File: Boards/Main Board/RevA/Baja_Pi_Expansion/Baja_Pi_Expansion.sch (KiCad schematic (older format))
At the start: 13 parts

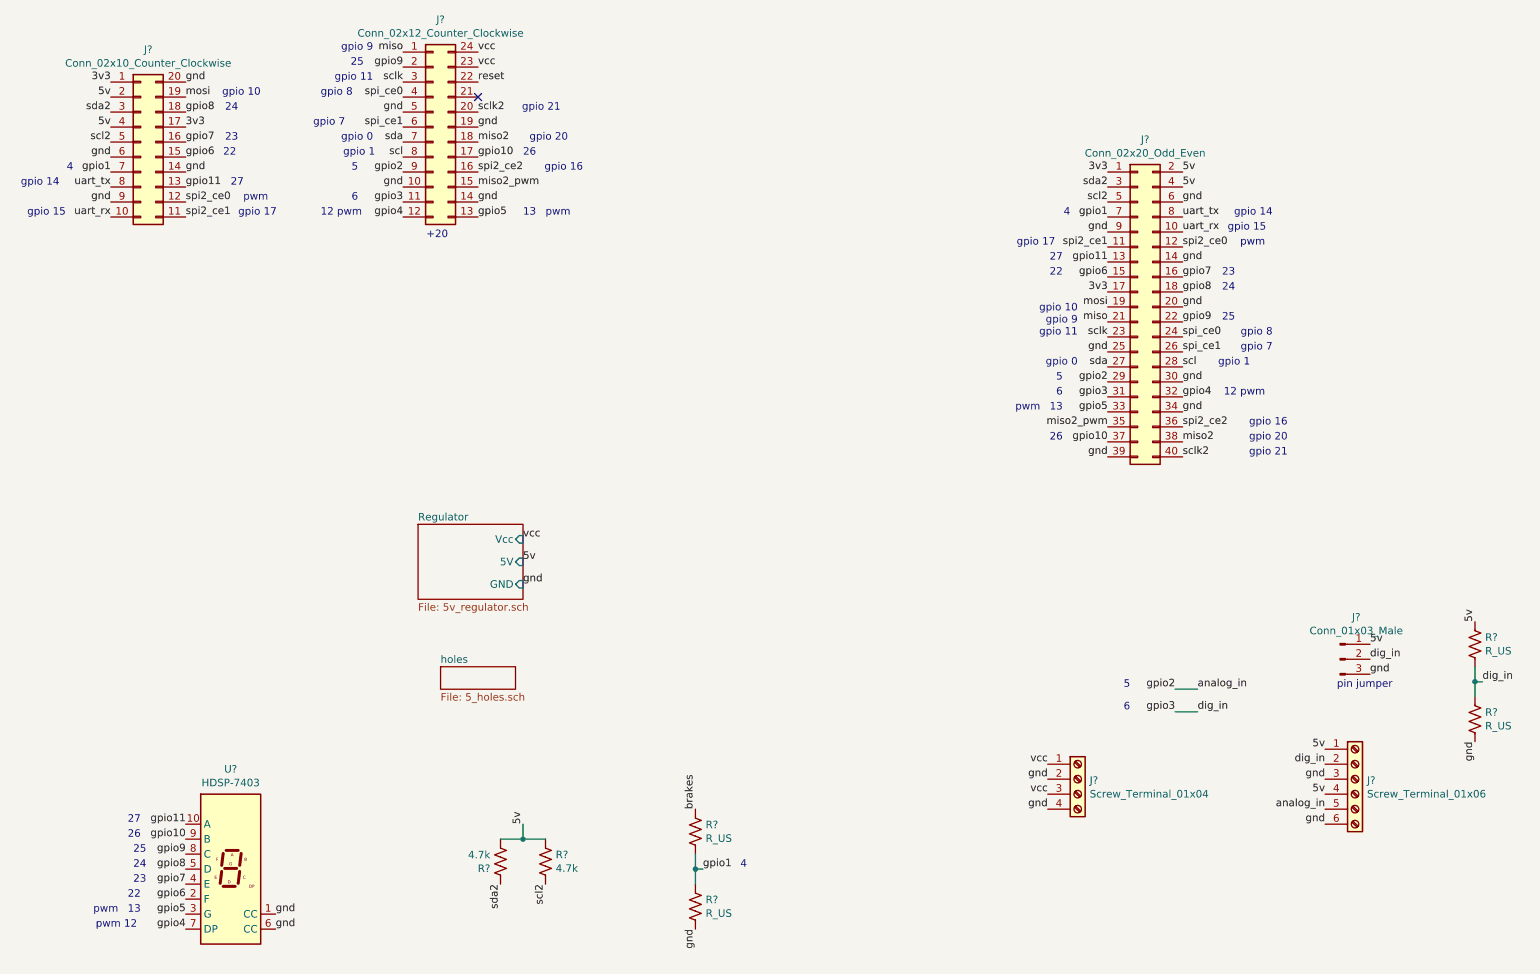
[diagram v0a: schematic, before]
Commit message: Added a Majority of Main Board Footprints
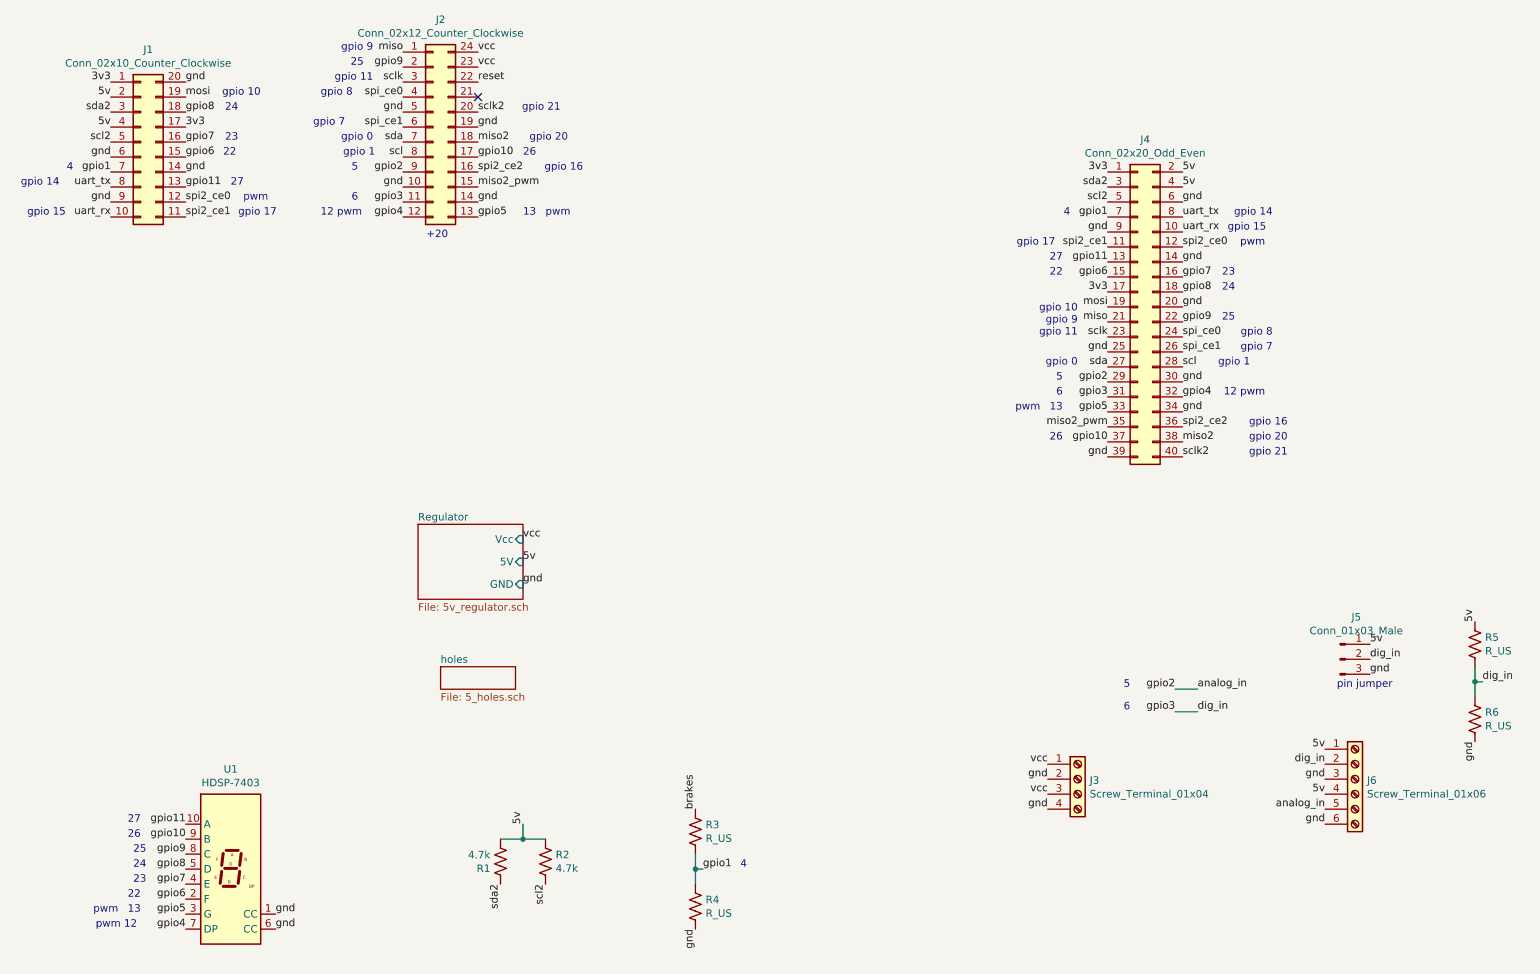
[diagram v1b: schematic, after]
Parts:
- J1: renamed from J?; footprint (none) -> Connector_PinHeader_2.54mm:PinHeader_2x10_P2.54mm_Vertical
- J2: renamed from J?; footprint (none) -> Connector_PinHeader_2.54mm:PinHeader_2x12_P2.54mm_Vertical
- J3: renamed from J?; footprint (none) -> Connector_PinHeader_2.54mm:PinHeader_1x04_P2.54mm_Vertical
- J4: renamed from J?; footprint (none) -> Connector_PinHeader_2.54mm:PinHeader_2x20_P2.54mm_Vertical
- J5: renamed from J?; footprint (none) -> Connector_PinHeader_2.54mm:PinHeader_1x03_P2.54mm_Vertical
- J6: renamed from J?; footprint (none) -> Connector_PinHeader_2.54mm:PinHeader_1x06_P2.54mm_Vertical
- R1, R2, R3, R4, R5, R6: renamed from R?; footprint (none) -> Resistor_SMD:R_0603_1608Metric
- gave numbers to parts that had none: 1
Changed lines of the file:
@@
 $EndDescr
 $Comp
-L Connector_Generic:Conn_02x20_Odd_Even J?
+L Connector_Generic:Conn_02x20_Odd_Even J4
 U 1 1 615F9685
 P 8550 2850
-F 0 "J?" H 8600 3967 50  0000 C CNN
+F 0 "J4" H 8600 3967 50  0000 C CNN
 F 1 "Conn_02x20_Odd_Even" H 8600 3876 50  0000 C CNN
-F 2 "" H 8550 2850 50  0001 C CNN
+F 2 "Connector_PinHeader_2.54mm:PinHeader_2x20_P2.54mm_Vertical" H 8550 2850 50  0001 C CNN
 F 3 "~" H 8550 2850 50  0001 C CNN
 	1    8550 2850
@@
 gpio 0
 $Comp
-L Connector_Generic:Conn_02x10_Counter_Clockwise J?
+L Connector_Generic:Conn_02x10_Counter_Clockwise J1
 U 1 1 6160E35B
 P 1900 1750
-F 0 "J?" H 1950 2367 50  0000 C CNN
+F 0 "J1" H 1950 2367 50  0000 C CNN
 F 1 "Conn_02x10_Counter_Clockwise" H 1950 2276 50  0000 C CNN
-F 2 "" H 1900 1750 50  0001 C CNN
+F 2 "Connector_PinHeader_2.54mm:PinHeader_2x10_P2.54mm_Vertical" H 1900 1750 50  0001 C CNN
 F 3 "~" H 1900 1750 50  0001 C CNN
 	1    1900 1750
@@
 $EndComp
 $Comp
-L Connector_Generic:Conn_02x12_Counter_Clockwise J?
+L Connector_Generic:Conn_02x12_Counter_Clockwise J2
 U 1 1 6160FED6
 P 3850 1650
-F 0 "J?" H 3900 2367 50  0000 C CNN
+F 0 "J2" H 3900 2367 50  0000 C CNN
 F 1 "Conn_02x12_Counter_Clockwise" H 3900 2276 50  0000 C CNN
-F 2 "" H 3850 1650 50  0001 C CNN
+F 2 "Connector_PinHeader_2.54mm:PinHeader_2x12_P2.54mm_Vertical" H 3850 1650 50  0001 C CNN
 F 3 "~" H 3850 1650 50  0001 C CNN
 	1    3850 1650
@@
 vcc
 $Comp
-L Display_Character:HDSP-7403 U?
+L Display_Character:HDSP-7403 U1
 U 1 1 61621AB7
 P 2500 6600
-F 0 "U?" H 2500 7267 50  0000 C CNN
+F 0 "U1" H 2500 7267 50  0000 C CNN
 F 1 "HDSP-7403" H 2500 7176 50  0000 C CNN
 F 2 "Display_7Segment:HDSP-7401" H 2500 6050 50  0001 C CNN
@@
 scl2
 $Comp
-L Device:R_US R?
+L Device:R_US R1
 U 1 1 6162B2A1
 P 4300 6550
-F 0 "R?" H 4232 6504 50  0000 R CNN
+F 0 "R1" H 4232 6504 50  0000 R CNN
 F 1 "4.7k" H 4232 6595 50  0000 R CNN
-F 2 "" V 4340 6540 50  0001 C CNN
+F 2 "Resistor_SMD:R_0603_1608Metric" V 4340 6540 50  0001 C CNN
 F 3 "~" H 4300 6550 50  0001 C CNN
 	1    4300 6550
@@
 $EndComp
 $Comp
-L Device:R_US R?
+L Device:R_US R2
 U 1 1 6162C8FC
 P 4600 6550
-F 0 "R?" H 4532 6504 50  0000 R CNN
+F 0 "R2" H 4532 6504 50  0000 R CNN
 F 1 "4.7k" H 4532 6595 50  0000 R CNN
-F 2 "" V 4640 6540 50  0001 C CNN
+F 2 "Resistor_SMD:R_0603_1608Metric" V 4640 6540 50  0001 C CNN
 F 3 "~" H 4600 6550 50  0001 C CNN
 	1    4600 6550
@@
 	4450 6400 4600 6400
 $Comp
-L Device:R_US R?
+L Device:R_US R3
 U 1 1 6162DB16
 P 5600 6350
-F 0 "R?" H 5668 6396 50  0000 L CNN
+F 0 "R3" H 5668 6396 50  0000 L CNN
 F 1 "R_US" H 5668 6305 50  0000 L CNN
-F 2 "" V 5640 6340 50  0001 C CNN
+F 2 "Resistor_SMD:R_0603_1608Metric" V 5640 6340 50  0001 C CNN
 F 3 "~" H 5600 6350 50  0001 C CNN
 	1    5600 6350
@@
 $EndComp
 $Comp
-L Device:R_US R?
+L Device:R_US R4
 U 1 1 6162E182
 P 5600 6850
-F 0 "R?" H 5668 6896 50  0000 L CNN
+F 0 "R4" H 5668 6896 50  0000 L CNN
 F 1 "R_US" H 5668 6805 50  0000 L CNN
-F 2 "" V 5640 6840 50  0001 C CNN
+F 2 "Resistor_SMD:R_0603_1608Metric" V 5640 6840 50  0001 C CNN
 F 3 "~" H 5600 6850 50  0001 C CNN
 	1    5600 6850
@@
 	5600 6600 5600 6500
 $Comp
-L Connector:Screw_Terminal_01x06 J?
+L Connector:Screw_Terminal_01x06 J6
 U 1 1 61634923
 P 10000 6000
-F 0 "J?" H 10080 5992 50  0000 L CNN
+F 0 "J6" H 10080 5992 50  0000 L CNN
 F 1 "Screw_Terminal_01x06" H 10080 5901 50  0000 L CNN
-F 2 "" H 10000 6000 50  0001 C CNN
+F 2 "Connector_PinHeader_2.54mm:PinHeader_1x06_P2.54mm_Vertical" H 10000 6000 50  0001 C CNN
 F 3 "~" H 10000 6000 50  0001 C CNN
 	1    10000 6000
@@
 $EndComp
 $Comp
-L Connector:Screw_Terminal_01x04 J?
+L Connector:Screw_Terminal_01x04 J3
 U 1 1 61635B3A
 P 8150 6000
-F 0 "J?" H 8230 5992 50  0000 L CNN
+F 0 "J3" H 8230 5992 50  0000 L CNN
 F 1 "Screw_Terminal_01x04" H 8230 5901 50  0000 L CNN
-F 2 "" H 8150 6000 50  0001 C CNN
+F 2 "Connector_PinHeader_2.54mm:PinHeader_1x04_P2.54mm_Vertical" H 8150 6000 50  0001 C CNN
 F 3 "~" H 8150 6000 50  0001 C CNN
 	1    8150 6000
@@
 vcc
 $Comp
-L Connector:Conn_01x03_Male J?
+L Connector:Conn_01x03_Male J5
 U 1 1 61637A7E
 P 9900 5200
-F 0 "J?" H 10008 5481 50  0000 C CNN
+F 0 "J5" H 10008 5481 50  0000 C CNN
 F 1 "Conn_01x03_Male" H 10008 5390 50  0000 C CNN
-F 2 "" H 9900 5200 50  0001 C CNN
+F 2 "Connector_PinHeader_2.54mm:PinHeader_1x03_P2.54mm_Vertical" H 9900 5200 50  0001 C CNN
 F 3 "~" H 9900 5200 50  0001 C CNN
 	1    9900 5200
@@
 analog_in
 $Comp
-L Device:R_US R?
+L Device:R_US R5
 U 1 1 6163FA23
 P 10800 5100
-F 0 "R?" H 10868 5146 50  0000 L CNN
+F 0 "R5" H 10868 5146 50  0000 L CNN
 F 1 "R_US" H 10868 5055 50  0000 L CNN
-F 2 "" V 10840 5090 50  0001 C CNN
+F 2 "Resistor_SMD:R_0603_1608Metric" V 10840 5090 50  0001 C CNN
 F 3 "~" H 10800 5100 50  0001 C CNN
 	1    10800 5100
@@
 $EndComp
 $Comp
-L Device:R_US R?
+L Device:R_US R6
 U 1 1 6163FA29
 P 10800 5600
-F 0 "R?" H 10868 5646 50  0000 L CNN
+F 0 "R6" H 10868 5646 50  0000 L CNN
 F 1 "R_US" H 10868 5555 50  0000 L CNN
-F 2 "" V 10840 5590 50  0001 C CNN
+F 2 "Resistor_SMD:R_0603_1608Metric" V 10840 5590 50  0001 C CNN
 F 3 "~" H 10800 5600 50  0001 C CNN
 	1    10800 5600

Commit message: Added \#Parts
(For 5V Regulator)
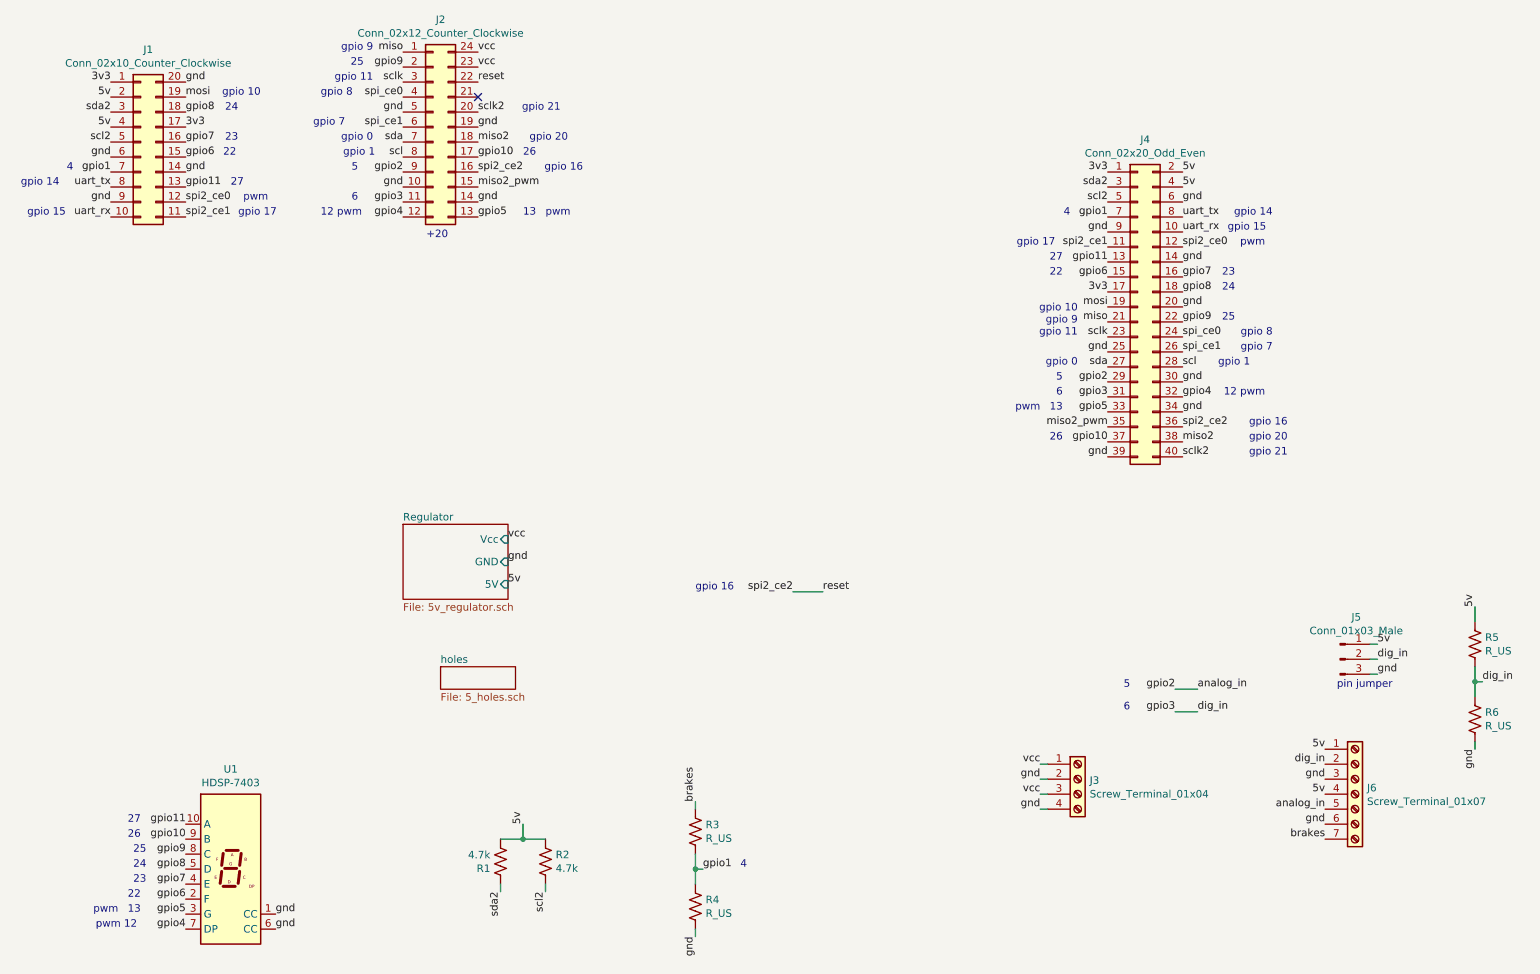
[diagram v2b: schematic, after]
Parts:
- removed J6: Screw_Terminal_01x06, Connector_PinHeader_2.54mm:PinHeader_1x06_P2.54mm_Vertical, symbol Connector:Screw_Terminal_01x06
- added J6: Screw_Terminal_01x07, Connector_PinHeader_2.54mm:PinHeader_1x07_P2.54mm_Vertical, symbol Connector:Screw_Terminal_01x07
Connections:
- net spi2_ce2 is gone; now on net reset: J2.16 (Pin_16), J4.36 (Pin_36)
- net 5v: now also J6.1 (Pin_1), J6.4 (Pin_4)
- net analog_in: now also J6.5 (Pin_5)
- net brakes: now also J6.7 (Pin_7)
- net dig_in: now also J6.2 (Pin_2)
- net gnd: now also J6.3 (Pin_3), J6.6 (Pin_6)
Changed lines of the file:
@@
 Text Notes 1600 7000 0    50   ~ 0
 pwm 12
-Text Label 4300 6700 3    50   ~ 0
+Text Label 4300 6750 3    50   ~ 0
 sda2
-Text Label 4600 6700 3    50   ~ 0
+Text Label 4600 6750 3    50   ~ 0
 scl2
 $Comp
@@
 Wire Wire Line
 	5600 6700 5600 6600
-Text Label 5600 7000 3    50   ~ 0
-gnd
-Text Label 5600 6200 1    50   ~ 0
+Text Label 5600 7050 3    50   ~ 0
+gnd
+Text Label 5600 6150 1    50   ~ 0
 brakes
 Text Label 5650 6600 0    50   ~ 0
@@
 Wire Wire Line
 	5600 6600 5600 6500
-$Comp
-L Connector:Screw_Terminal_01x06 J6
-U 1 1 61634923
-P 10000 6000
-F 0 "J6" H 10080 5992 50  0000 L CNN
-F 1 "Screw_Terminal_01x06" H 10080 5901 50  0000 L CNN
-F 2 "Connector_PinHeader_2.54mm:PinHeader_1x06_P2.54mm_Vertical" H 10000 6000 50  0001 C CNN
-F 3 "~" H 10000 6000 50  0001 C CNN
-	1    10000 6000
-	1    0    0    -1
-$EndComp
 $Comp
 L Connector:Screw_Terminal_01x04 J3
@@
 	1    0    0    -1
 $EndComp
-Text Label 7950 6000 2    50   ~ 0
-gnd
-Text Label 7950 6200 2    50   ~ 0
-gnd
-Text Label 7950 5900 2    50   ~ 0
+Text Label 7900 6000 2    50   ~ 0
+gnd
+Text Label 7900 6200 2    50   ~ 0
+gnd
+Text Label 7900 5900 2    50   ~ 0
 vcc
-Text Label 7950 6100 2    50   ~ 0
+Text Label 7900 6100 2    50   ~ 0
 vcc
 $Comp
@@
 Text Label 9800 6000 2    50   ~ 0
 gnd
-Text Label 10100 5300 0    50   ~ 0
-gnd
-Text Label 10100 5200 0    50   ~ 0
-dig_in
-Text Label 10100 5100 0    50   ~ 0
+Text Label 10150 5300 0    50   ~ 0
+gnd
+Text Label 10150 5200 0    50   ~ 0
+dig_in
+Text Label 10150 5100 0    50   ~ 0
 5v
 Text Label 9800 5800 2    50   ~ 0
@@
 Text Label 10850 5350 0    50   ~ 0
 dig_in
-Text Label 10800 4950 1    50   ~ 0
-5v
-Text Label 10800 5750 3    50   ~ 0
+Text Label 10800 4850 1    50   ~ 0
+5v
+Text Label 10800 5800 3    50   ~ 0
 gnd
 Text Label 8800 5400 2    50   ~ 0
@@
 pin jumper
 $Sheet
-S 3750 4300 700  500
+S 3650 4300 700  500
 U 6164E083
 F0 "Regulator" 50
 F1 "5v_regulator.sch" 50
-F2 "Vcc" I R 4450 4400 50
-F3 "5V" I R 4450 4550 50
-F4 "GND" I R 4450 4700 50
+F2 "Vcc" I R 4350 4400 50
+F3 "GND" I R 4350 4550 50
+F4 "5V" I R 4350 4700 50
 $EndSheet
-Text Label 4450 4700 0    50   ~ 0
-gnd
-Text Label 4450 4400 0    50   ~ 0
+Text Label 4350 4550 0    50   ~ 0
+gnd
+Text Label 4350 4400 0    50   ~ 0
 vcc
-Text Label 4450 4550 0    50   ~ 0
+Text Label 4350 4700 0    50   ~ 0
 5v
 $Sheet
@@
 F1 "5_holes.sch" 50
 $EndSheet
+Text Label 6450 4750 0    50   ~ 0
+reset
+Text Label 6250 4750 2    50   ~ 0
+spi2_ce2
+Text Notes 5600 4750 0    50   ~ 0
+gpio 16
+$Comp
+L Connector:Screw_Terminal_01x07 J6
+U 1 1 61673830
+P 10000 6100
+F 0 "J6" H 10080 6142 50  0000 L CNN
+F 1 "Screw_Terminal_01x07" H 10080 6051 50  0000 L CNN
+F 2 "Connector_PinHeader_2.54mm:PinHeader_1x07_P2.54mm_Vertical" H 10000 6100 50  0001 C CNN
+F 3 "~" H 10000 6100 50  0001 C CNN
+	1    10000 6100
+	1    0    0    -1
+$EndComp
+Text Label 9800 6400 2    50   ~ 0
+brakes
+Wire Wire Line
+	6250 4750 6450 4750
+Wire Wire Line
+	4300 6750 4300 6700
+Wire Wire Line
+	4600 6750 4600 6700
+Wire Wire Line
+	5600 6150 5600 6200
+Wire Wire Line
+	5600 7050 5600 7000
+Wire Wire Line
+	10150 5100 10100 5100
+Wire Wire Line
+	10150 5200 10100 5200
+Wire Wire Line
+	10150 5300 10100 5300
+Wire Wire Line
+	10800 4950 10800 4850
+Wire Wire Line
+	10800 5800 10800 5750
+Wire Wire Line
+	7900 5900 7950 5900
+Wire Wire Line
+	7950 6000 7900 6000
+Wire Wire Line
+	7900 6100 7950 6100
+Wire Wire Line
+	7950 6200 7900 6200
 $EndSCHEMATC
